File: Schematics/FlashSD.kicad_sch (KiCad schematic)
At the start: 3 parts, among them J3 Micro_SD_Card

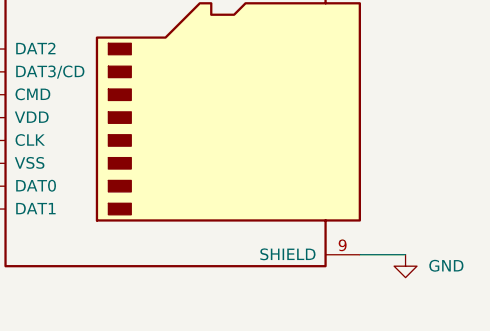
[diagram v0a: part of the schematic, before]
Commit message: added esp32 for uart to tune control systems from a web browser app
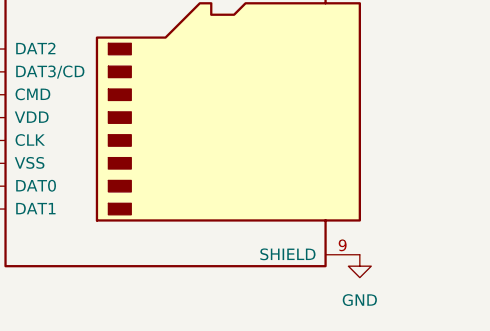
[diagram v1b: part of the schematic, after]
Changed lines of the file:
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@@
-	(wire
-		(pts
-			(xy 204.47 111.76) (xy 199.39 111.76)
-		)
-		(stroke
-			(width 0)
-			(type default)
-		)
-	)
 	(wire
 		(pts
@@
 				(path "/8a3e7f99-4046-40e8-bd7c-d9d1c8c7162e/90a33a35-ba22-452a-8971-c9b1cdf9eace"
 					(reference "#PWR064")
-					(unit 1)
-				)
-			)
-		)
-	)
-	(symbol
-		(lib_id "power:GND")
-		(at 204.47 111.76 0)
-		(unit 1)
-		(exclude_from_sim no)
-		(in_bom yes)
-		(on_board yes)
-		(dnp no)
-		(fields_autoplaced yes)
-		(property "Reference" "#PWR066"
-			(at 204.47 118.11 0)
-			(effects
-				(font
-					(size 1.27 1.27)
-				)
-				(hide yes)
-			)
-		)
-		(property "Value" "GND"
-			(at 207.01 113.0299 0)
-			(effects
-				(font
-					(size 1.27 1.27)
-				)
-				(justify left)
-			)
-		)
-		(property "Footprint" ""
-			(at 204.47 111.76 0)
-			(effects
-				(font
-					(size 1.27 1.27)
-				)
-				(hide yes)
-			)
-		)
-		(property "Datasheet" ""
-			(at 204.47 111.76 0)
-			(effects
-				(font
-					(size 1.27 1.27)
-				)
-				(hide yes)
-			)
-		)
-		(property "Description" "Power symbol creates a global label with name \"GND\" , ground"
-			(at 204.47 111.76 0)
-			(effects
-				(font
-					(size 1.27 1.27)
-				)
-				(hide yes)
-			)
-		)
-		(pin "1"
-		)
-		(instances
-			(project "CAN-Interface-Board"
-				(path "/8a3e7f99-4046-40e8-bd7c-d9d1c8c7162e/90a33a35-ba22-452a-8971-c9b1cdf9eace"
-					(reference "#PWR066")
 					(unit 1)
 				)
@@
 					(unit 1)
 				)
+			)
+		)
+	)
+	(symbol
+		(lib_id "power:GND")
+		(at 199.39 111.76 0)
+		(unit 1)
+		(exclude_from_sim no)
+		(in_bom yes)
+		(on_board yes)
+		(dnp no)
+		(fields_autoplaced yes)
+		(property "Reference" "#PWR03"
+			(at 199.39 118.11 0)
+			(effects
+				(font
+					(size 1.27 1.27)
+				)
+				(hide yes)
+			)
+		)
+		(property "Value" "GND"
+			(at 199.39 116.84 0)
+			(effects
+				(font
+					(size 1.27 1.27)
+				)
+			)
+		)
+		(property "Footprint" ""
+			(at 199.39 111.76 0)
+			(effects
+				(font
+					(size 1.27 1.27)
+				)
+				(hide yes)
+			)
+		)
+		(property "Datasheet" ""
+			(at 199.39 111.76 0)
+			(effects
+				(font
+					(size 1.27 1.27)
+				)
+				(hide yes)
+			)
+		)
+		(property "Description" "Power symbol creates a global label with name \"GND\" , ground"
+			(at 199.39 111.76 0)
+			(effects
+				(font
+					(size 1.27 1.27)
+				)
+				(hide yes)
+			)
+		)
+		(pin "1"
+		)
+		(instances
+			(project "CAN-Interface-Board"
+				(path "/8a3e7f99-4046-40e8-bd7c-d9d1c8c7162e/90a33a35-ba22-452a-8971-c9b1cdf9eace"
+					(reference "#PWR03")
+					(unit 1)
+				)

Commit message: final draft, in JLPCB cart
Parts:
- J3: footprint Connector_Card:microSD_HC_Molex_104031-0811 -> Connector_Card:microSD_HC_Molex_47219-2001
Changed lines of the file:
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@@
 			)
 		)
-		(property "Description" "Resistor"
-			(at 133.35 91.44 0)
+		(property "Description" ""
+			(at 133.35 91.44 90)
 			(hide yes)
 			(show_name no)
@@
 		)
 		(property "LCSC" "C84376"
+			(at 133.35 91.44 90)
+			(hide yes)
+			(show_name no)
+			(do_not_autoplace no)
+			(effects
+				(font
+					(size 1.27 1.27)
+				)
+			)
+		)
+		(property "SnapEDA_Link" ""
+			(at 133.35 91.44 90)
+			(hide yes)
+			(show_name no)
+			(do_not_autoplace no)
+			(effects
+				(font
+					(size 1.27 1.27)
+				)
+			)
+		)
+		(property "DESCRIPTION" ""
 			(at 133.35 91.44 90)
 			(hide yes)
@@
 			)
 		)
-		(property "Description" "Resistor"
-			(at 118.11 99.06 0)
+		(property "Description" ""
+			(at 118.11 99.06 90)
 			(hide yes)
 			(show_name no)
@@
 		)
 		(property "LCSC" "C126353"
+			(at 118.11 99.06 90)
+			(hide yes)
+			(show_name no)
+			(do_not_autoplace no)
+			(effects
+				(font
+					(size 1.27 1.27)
+				)
+			)
+		)
+		(property "SnapEDA_Link" ""
+			(at 118.11 99.06 90)
+			(hide yes)
+			(show_name no)
+			(do_not_autoplace no)
+			(effects
+				(font
+					(size 1.27 1.27)
+				)
+			)
+		)
+		(property "DESCRIPTION" ""
 			(at 118.11 99.06 90)
 			(hide yes)
@@
 			)
 		)
-		(property "Footprint" "Connector_Card:microSD_HC_Molex_104031-0811"
+		(property "Footprint" "Connector_Card:microSD_HC_Molex_47219-2001"
 			(at 208.28 88.9 0)
 			(hide yes)
@@
 			)
 		)
-		(property "Description" "Micro SD Card Socket"
+		(property "Description" ""
 			(at 179.07 96.52 0)
 			(hide yes)
@@
 			(at 179.07 96.52 0)
 			(hide yes)
+			(show_name no)
+			(do_not_autoplace no)
+			(effects
+				(font
+					(size 1.27 1.27)
+				)
+			)
+		)
+		(property "SnapEDA_Link" ""
+			(at 179.07 96.52 0)
+			(hide yes)
+			(show_name no)
+			(do_not_autoplace no)
+			(effects
+				(font
+					(size 1.27 1.27)
+				)
+			)
+		)
+		(property "DESCRIPTION" ""
+			(at 179.07 96.52 0)
+			(hide yes)

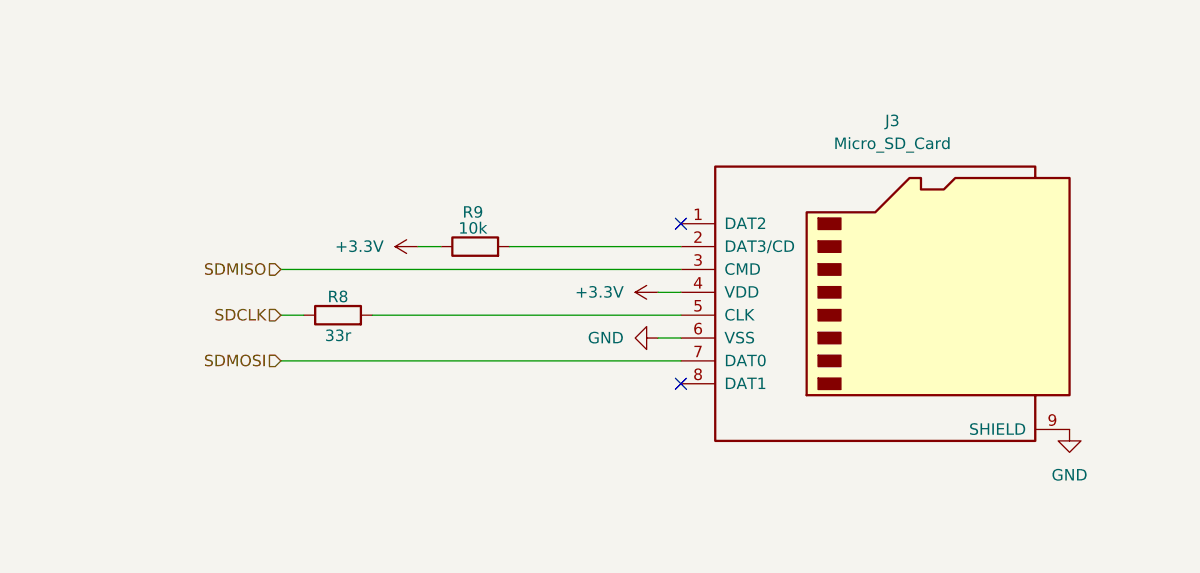
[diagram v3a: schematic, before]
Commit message: Added encoder connection for parafoil motor position information, in buy order ready for purchase
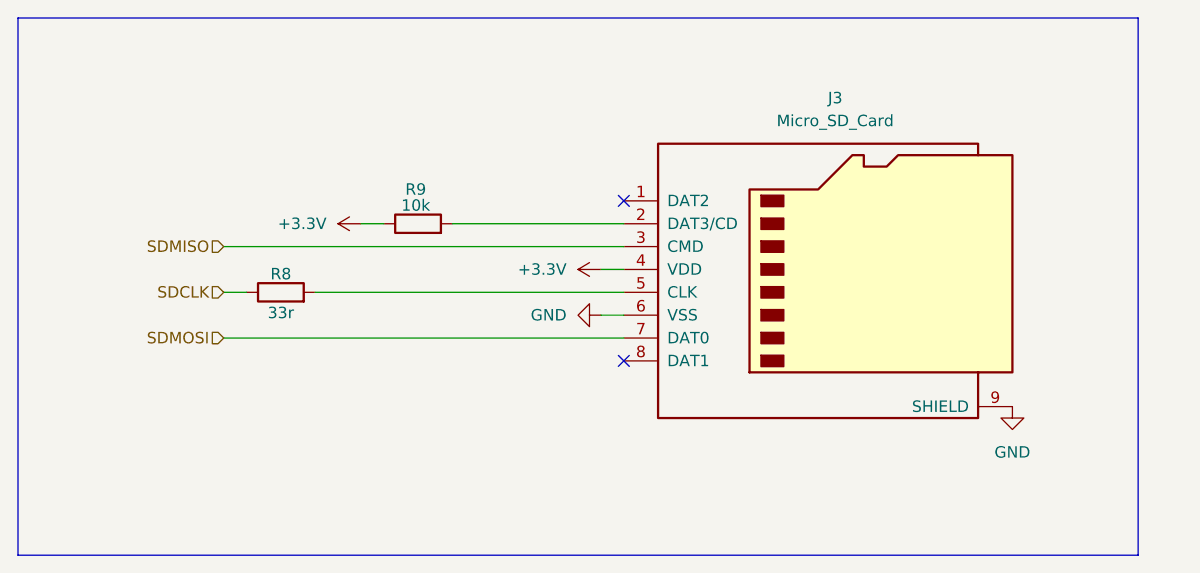
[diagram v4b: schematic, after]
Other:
- moved on the sheet: J3, R8, R9
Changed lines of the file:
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@@
 	(generator_version "10.0")
 	(paper "A4")
+	(rectangle
+		(start 82.55 66.04)
+		(end 207.01 125.73)
+		(stroke
+			(width 0)
+			(type default)
+		)
+		(fill
+			(type none)
+		)
+	)
 	(no_connect
-		(at 156.21 88.9)
+		(at 149.86 86.36)
 	)
 	(no_connect
-		(at 156.21 106.68)
+		(at 149.86 104.14)
 	)
 	(wire
 		(pts
-			(xy 111.76 93.98) (xy 156.21 93.98)
+			(xy 105.41 91.44) (xy 149.86 91.44)
 		)
 		(stroke
@@
 	(wire
 		(pts
-			(xy 153.67 96.52) (xy 156.21 96.52)
+			(xy 147.32 93.98) (xy 149.86 93.98)
 		)
 		(stroke
@@
 	(wire
 		(pts
-			(xy 127 91.44) (xy 129.54 91.44)
+			(xy 120.65 88.9) (xy 123.19 88.9)
 		)
 		(stroke
@@
 	(wire
 		(pts
-			(xy 111.76 104.14) (xy 156.21 104.14)
+			(xy 105.41 101.6) (xy 149.86 101.6)
 		)
 		(stroke
@@
 	(wire
 		(pts
-			(xy 121.92 99.06) (xy 156.21 99.06)
+			(xy 115.57 96.52) (xy 149.86 96.52)
 		)
 		(stroke
@@
 	(wire
 		(pts
-			(xy 153.67 101.6) (xy 156.21 101.6)
+			(xy 147.32 99.06) (xy 149.86 99.06)
 		)
 		(stroke
@@
 	(wire
 		(pts
-			(xy 137.16 91.44) (xy 156.21 91.44)
+			(xy 130.81 88.9) (xy 149.86 88.9)
 		)
 		(stroke
@@
 	(wire
 		(pts
-			(xy 111.76 99.06) (xy 114.3 99.06)
+			(xy 105.41 96.52) (xy 107.95 96.52)
 		)
 		(stroke
@@
 	(hierarchical_label "SDCLK"
 		(shape input)
-		(at 111.76 99.06 180)
+		(at 105.41 96.52 180)
 		(effects
 			(font
@@
 	(hierarchical_label "SDMOSI"
 		(shape input)
-		(at 111.76 104.14 180)
+		(at 105.41 101.6 180)
 		(effects
 			(font
@@
 	(hierarchical_label "SDMISO"
 		(shape input)
-		(at 111.76 93.98 180)
+		(at 105.41 91.44 180)
 		(effects
 			(font
@@
 	(symbol
 		(lib_id "power:+3.3V")
-		(at 153.67 96.52 90)
+		(at 147.32 93.98 90)
 		(unit 1)
 		(body_style 1)
@@
 		(dnp no)
 		(property "Reference" "#PWR064"
-			(at 157.48 96.52 0)
+			(at 151.13 93.98 0)
 			(hide yes)
 			(show_name no)
@@
 		)
 		(property "Value" "+3.3V"
-			(at 149.86 96.5199 90)
+			(at 143.51 93.9799 90)
 			(show_name no)
 			(do_not_autoplace no)
@@
 		)
 		(property "Footprint" ""
-			(at 153.67 96.52 0)
+			(at 147.32 93.98 0)
 			(hide yes)
 			(show_name no)
@@
 		)
 		(property "Datasheet" ""
-			(at 153.67 96.52 0)
+			(at 147.32 93.98 0)
 			(hide yes)
 			(show_name no)
@@
 		)
 		(property "Description" "Power symbol creates a global label with name \"+3.3V\""
-			(at 153.67 96.52 0)
+			(at 147.32 93.98 0)
 			(hide yes)
 			(show_name no)
@@
 	(symbol
 		(lib_id "Device:R")
-		(at 133.35 91.44 90)
+		(at 127 88.9 90)
 		(unit 1)
 		(body_style 1)
@@
 		(dnp no)
 		(property "Reference" "R9"
-			(at 133.096 87.63 90)
+			(at 126.746 85.09 90)
 			(show_name no)
 			(do_not_autoplace no)
@@
 		)
 		(property "Value" "10k"
-			(at 133.096 89.408 90)
+			(at 126.746 86.868 90)
 			(show_name no)
 			(do_not_autoplace no)
@@
 		)
 		(property "Footprint" "Resistor_SMD:R_0805_2012Metric_Pad1.20x1.40mm_HandSolder"
-			(at 133.35 93.218 90)
+			(at 127 90.678 90)
 			(hide yes)
 			(show_name no)
@@
 		)
 		(property "Datasheet" ""
-			(at 133.35 91.44 0)
+			(at 127 88.9 0)
 			(hide yes)
 			(show_name no)
@@
 		)
 		(property "Description" ""
-			(at 133.35 91.44 90)
+			(at 127 88.9 90)
 			(hide yes)
 			(show_name no)
@@
 		)
 		(property "LCSC Part" "C84376"
-			(at 133.35 91.44 90)
+			(at 127 88.9 90)
 			(hide yes)
 			(show_name no)
@@
 		)
 		(property "LCSC" "C84376"
-			(at 133.35 91.44 90)
+			(at 127 88.9 90)
 			(hide yes)
 			(show_name no)
@@
 		)
 		(property "SnapEDA_Link" ""
-			(at 133.35 91.44 90)
+			(at 127 88.9 90)
 			(hide yes)
 			(show_name no)
@@
 		)
 		(property "DESCRIPTION" ""
-			(at 133.35 91.44 90)
+			(at 127 88.9 90)
 			(hide yes)
 			(show_name no)
@@
 	(symbol
 		(lib_id "Device:R")
-		(at 118.11 99.06 90)
+		(at 111.76 96.52 90)
 		(unit 1)
 		(body_style 1)
@@
 		(dnp no)
 		(property "Reference" "R8"
-			(at 118.11 97.028 90)
+			(at 111.76 94.488 90)
 			(show_name no)
 			(do_not_autoplace no)
@@
 		)
 		(property "Value" "33r"
-			(at 118.11 101.346 90)
+			(at 111.76 98.806 90)
 			(show_name no)
 			(do_not_autoplace no)
@@
 		)
 		(property "Footprint" "Resistor_SMD:R_0805_2012Metric_Pad1.20x1.40mm_HandSolder"
-			(at 118.11 100.838 90)
+			(at 111.76 98.298 90)
 			(hide yes)
 			(show_name no)
@@
 		)
 		(property "Datasheet" ""
-			(at 118.11 99.06 0)
+			(at 111.76 96.52 0)
 			(hide yes)
 			(show_name no)
@@
 		)
 		(property "Description" ""
-			(at 118.11 99.06 90)
+			(at 111.76 96.52 90)
 			(hide yes)
 			(show_name no)
@@
 		)
 		(property "LCSC Part" "C17557"
-			(at 118.11 99.06 90)
+			(at 111.76 96.52 90)
 			(hide yes)
 			(show_name no)
@@
 		)
 		(property "LCSC" "C126353"
-			(at 118.11 99.06 90)
+			(at 111.76 96.52 90)
 			(hide yes)
 			(show_name no)
@@
 		)
 		(property "SnapEDA_Link" ""
-			(at 118.11 99.06 90)
+			(at 111.76 96.52 90)
 			(hide yes)
 			(show_name no)
@@
 		)
 		(property "DESCRIPTION" ""
-			(at 118.11 99.06 90)
+			(at 111.76 96.52 90)
 			(hide yes)
 			(show_name no)
@@
 	(symbol
 		(lib_id "power:GND")
-		(at 153.67 101.6 270)
+		(at 147.32 99.06 270)
 		(unit 1)
 		(body_style 1)
@@
 		(fields_autoplaced yes)
 		(property "Reference" "#PWR065"
-			(at 147.32 101.6 0)
+			(at 140.97 99.06 0)
 			(hide yes)
 			(show_name no)
@@
 		)
 		(property "Value" "GND"
-			(at 149.86 101.5999 90)
+			(at 143.51 99.0599 90)
 			(show_name no)
 			(do_not_autoplace no)
@@
 		)
 		(property "Footprint" ""
-			(at 153.67 101.6 0)
+			(at 147.32 99.06 0)
 			(hide yes)
 			(show_name no)
@@
 		)
 		(property "Datasheet" ""
-			(at 153.67 101.6 0)
+			(at 147.32 99.06 0)
 			(hide yes)
 			(show_name no)
@@
 		)
 		(property "Description" "Power symbol creates a global label with name \"GND\" , ground"
-			(at 153.67 101.6 0)
+			(at 147.32 99.06 0)
 			(hide yes)
 			(show_name no)
@@
 	(symbol
 		(lib_id "power:GND")
-		(at 199.39 111.76 0)
+		(at 193.04 109.22 0)
 		(unit 1)
 		(body_style 1)
@@
 		(fields_autoplaced yes)
 		(property "Reference" "#PWR03"
-			(at 199.39 118.11 0)
+			(at 193.04 115.57 0)
 			(hide yes)
 			(show_name no)
@@
 		)
 		(property "Value" "GND"
-			(at 199.39 116.84 0)
+			(at 193.04 114.3 0)
 			(show_name no)
 			(do_not_autoplace no)
@@
 		)
 		(property "Footprint" ""
-			(at 199.39 111.76 0)
+			(at 193.04 109.22 0)
 			(hide yes)
 			(show_name no)
@@
 		)
 		(property "Datasheet" ""
-			(at 199.39 111.76 0)
+			(at 193.04 109.22 0)
 			(hide yes)
 			(show_name no)
@@
 		)
 		(property "Description" "Power symbol creates a global label with name \"GND\" , ground"
-			(at 199.39 111.76 0)
+			(at 193.04 109.22 0)
 			(hide yes)
 			(show_name no)
@@
 	(symbol
 		(lib_id "Connector:Micro_SD_Card")
-		(at 179.07 96.52 0)
+		(at 172.72 93.98 0)
 		(unit 1)
 		(body_style 1)
@@
 		(fields_autoplaced yes)
 		(property "Reference" "J3"
-			(at 179.705 77.47 0)
+			(at 173.355 74.93 0)
 			(show_name no)
 			(do_not_autoplace no)
@@
 		)
 		(property "Value" "Micro_SD_Card"
-			(at 179.705 80.01 0)
+			(at 173.355 77.47 0)
 			(show_name no)
 			(do_not_autoplace no)
@@
 		)
 		(property "Footprint" "Connector_Card:microSD_HC_Molex_47219-2001"
-			(at 208.28 88.9 0)
+			(at 201.93 86.36 0)
 			(hide yes)
 			(show_name no)
@@
 		)
 		(property "Datasheet" "https://www.we-online.com/components/products/datasheet/693072010801.pdf"
-			(at 179.07 96.52 0)
+			(at 172.72 93.98 0)
 			(hide yes)
 			(show_name no)
@@
 		)
 		(property "Description" ""
-			(at 179.07 96.52 0)
+			(at 172.72 93.98 0)
 			(hide yes)
 			(show_name no)
@@
 		)
 		(property "LCSC Part" "C164170"
-			(at 179.07 96.52 0)
+			(at 172.72 93.98 0)
 			(hide yes)
 			(show_name no)
@@
 		)
 		(property "LCSC" "C164170"
-			(at 179.07 96.52 0)
+			(at 172.72 93.98 0)
 			(hide yes)
 			(show_name no)
@@
 		)
 		(property "SnapEDA_Link" ""
-			(at 179.07 96.52 0)
+			(at 172.72 93.98 0)
 			(hide yes)
 			(show_name no)
@@
 		)
 		(property "DESCRIPTION" ""
-			(at 179.07 96.52 0)
+			(at 172.72 93.98 0)
 			(hide yes)
 			(show_name no)
@@
 	(symbol
 		(lib_id "power:+3.3V")
-		(at 127 91.44 90)
+		(at 120.65 88.9 90)
 		(unit 1)
 		(body_style 1)
@@
 		(fields_autoplaced yes)
 		(property "Reference" "#PWR063"
-			(at 130.81 91.44 0)
+			(at 124.46 88.9 0)
 			(hide yes)
 			(show_name no)
@@
 		)
 		(property "Value" "+3.3V"
-			(at 123.19 91.4399 90)
+			(at 116.84 88.8999 90)
 			(show_name no)
 			(do_not_autoplace no)
@@
 		)
 		(property "Footprint" ""
-			(at 127 91.44 0)
+			(at 120.65 88.9 0)
 			(hide yes)
 			(show_name no)
@@
 		)
 		(property "Datasheet" ""
-			(at 127 91.44 0)
+			(at 120.65 88.9 0)
 			(hide yes)
 			(show_name no)
@@
 		)
 		(property "Description" "Power symbol creates a global label with name \"+3.3V\""
-			(at 127 91.44 0)
-			(hide yes)
-			(show_name no)
+			(at 120.65 88.9 0)
+			(hide yes)
+			(show_name no)
